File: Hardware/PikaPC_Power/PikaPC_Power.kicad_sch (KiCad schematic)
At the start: 14 parts, among them J1 ATX-24, J2 DIN41612_03x32_C_Split, J3 ATX-20, J4 Conn_01x02, J5 Conn_01x02, SW1 SW_Push_DPDT

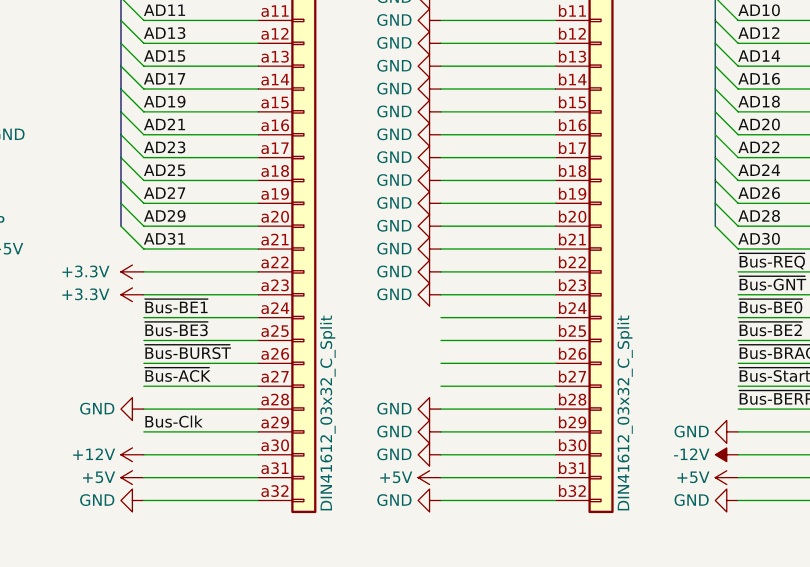
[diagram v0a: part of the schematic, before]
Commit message: Un-assign main bus pins 22 & 23
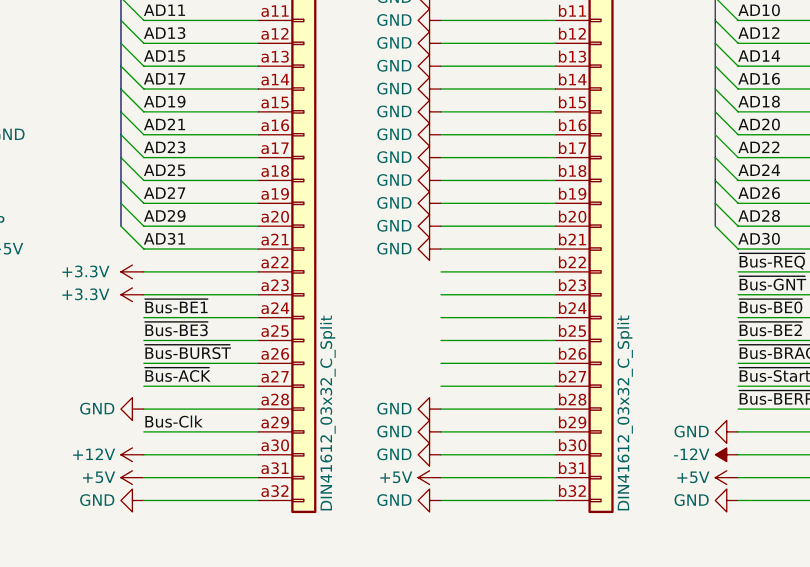
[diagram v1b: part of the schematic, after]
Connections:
- net GND: no longer J2.b22 (Pin_b22), J2.b23 (Pin_b23)
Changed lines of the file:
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@@
 	(symbol
 		(lib_id "power:GND")
-		(at 208.28 78.74 270)
-		(unit 1)
-		(exclude_from_sim no)
-		(in_bom yes)
-		(on_board yes)
-		(dnp no)
-		(fields_autoplaced yes)
-		(property "Reference" "#PWR0148"
-			(at 201.93 78.74 0)
-			(effects
-				(font
-					(size 1.27 1.27)
-				)
-				(hide yes)
-			)
-		)
-		(property "Value" "GND"
-			(at 205.1051 78.74 90)
-			(effects
-				(font
-					(size 1.27 1.27)
-				)
-				(justify right)
-			)
-		)
-		(property "Footprint" ""
-			(at 208.28 78.74 0)
-			(effects
-				(font
-					(size 1.27 1.27)
-				)
-				(hide yes)
-			)
-		)
-		(property "Datasheet" ""
-			(at 208.28 78.74 0)
-			(effects
-				(font
-					(size 1.27 1.27)
-				)
-				(hide yes)
-			)
-		)
-		(property "Description" "Power symbol creates a global label with name \"GND\" , ground"
-			(at 208.28 78.74 0)
-			(effects
-				(font
-					(size 1.27 1.27)
-				)
-				(hide yes)
-			)
-		)
-		(pin "1"
-		)
-		(instances
-			(project "PikaPC_Power"
-				(path "/840b0ed4-db56-4e24-ac62-6fd5c14b7777"
-					(reference "#PWR0148")
-					(unit 1)
-				)
-			)
-		)
-	)
-	(symbol
-		(lib_id "power:GND")
 		(at 101.6 152.4 0)
 		(unit 1)
@@
 					(unit 1)
 				)
-			)
-		)
-	)
-	(symbol
-		(lib_id "power:GND")
-		(at 208.28 81.28 270)
-		(unit 1)
-		(exclude_from_sim no)
-		(in_bom yes)
-		(on_board yes)
-		(dnp no)
-		(fields_autoplaced yes)
-		(property "Reference" "#PWR0149"
-			(at 201.93 81.28 0)
-			(effects
-				(font
-					(size 1.27 1.27)
-				)
-				(hide yes)
-			)
-		)
-		(property "Value" "GND"
-			(at 205.1051 81.28 90)
-			(effects
-				(font
-					(size 1.27 1.27)
-				)
-				(justify right)
-			)
-		)
-		(property "Footprint" ""
-			(at 208.28 81.28 0)
-			(effects
-				(font
-					(size 1.27 1.27)
-				)
-				(hide yes)
-			)
-		)
-		(property "Datasheet" ""
-			(at 208.28 81.28 0)
-			(effects
-				(font
-					(size 1.27 1.27)
-				)
-				(hide yes)
-			)
-		)
-		(property "Description" "Power symbol creates a global label with name \"GND\" , ground"
-			(at 208.28 81.28 0)
-			(effects
-				(font
-					(size 1.27 1.27)
-				)
-				(hide yes)
-			)
-		)
-		(pin "1"
-		)
-		(instances
-			(project "PikaPC_Power"
-				(path "/840b0ed4-db56-4e24-ac62-6fd5c14b7777"
-					(reference "#PWR0149")
-					(unit 1)
-				)
